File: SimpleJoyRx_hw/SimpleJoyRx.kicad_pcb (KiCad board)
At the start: 2 copper layers, 20 x 50 mm, 111 parts, among them Q1 IRF9358, Q2 2N7002, Q3 IRLML0030, Q4 IRLML0030, SW1 DIPx8, SW2 BUTTON, SW3 1P2T, U1 USBLC6

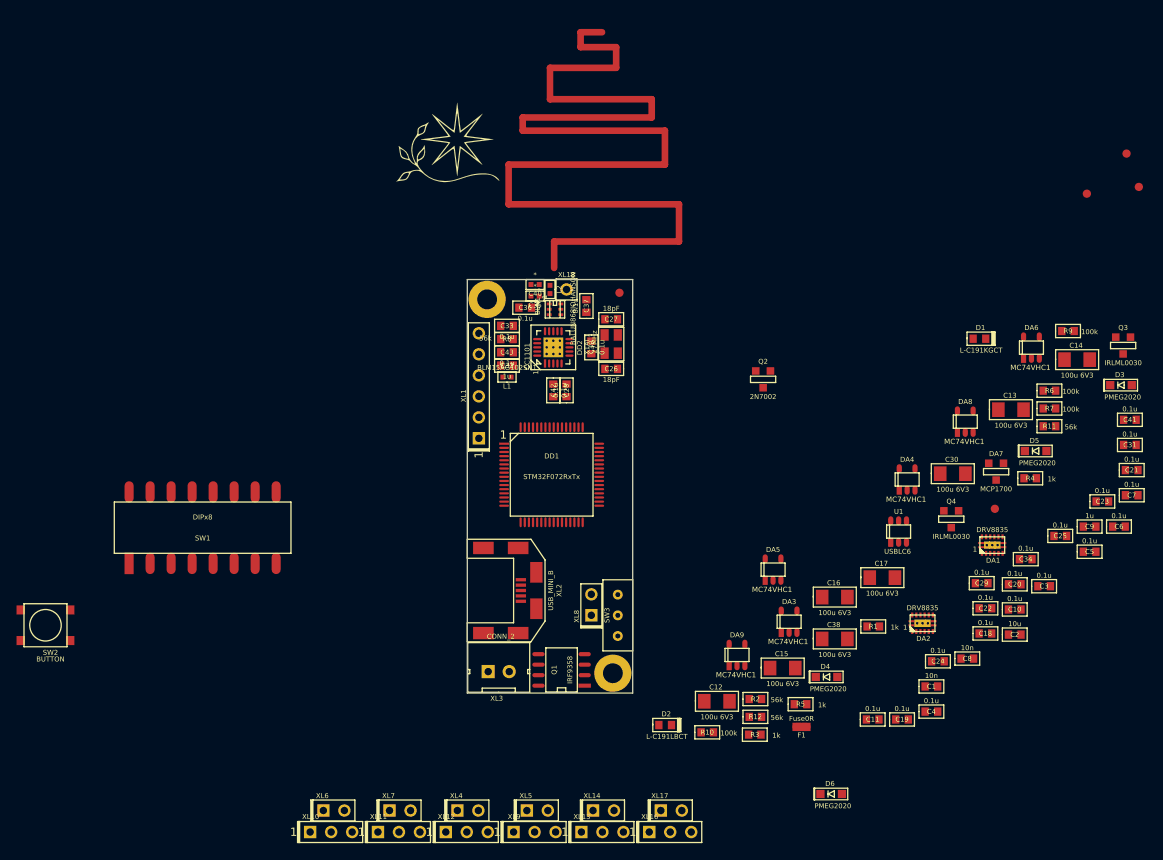
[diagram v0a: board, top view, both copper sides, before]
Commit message: RX layout done
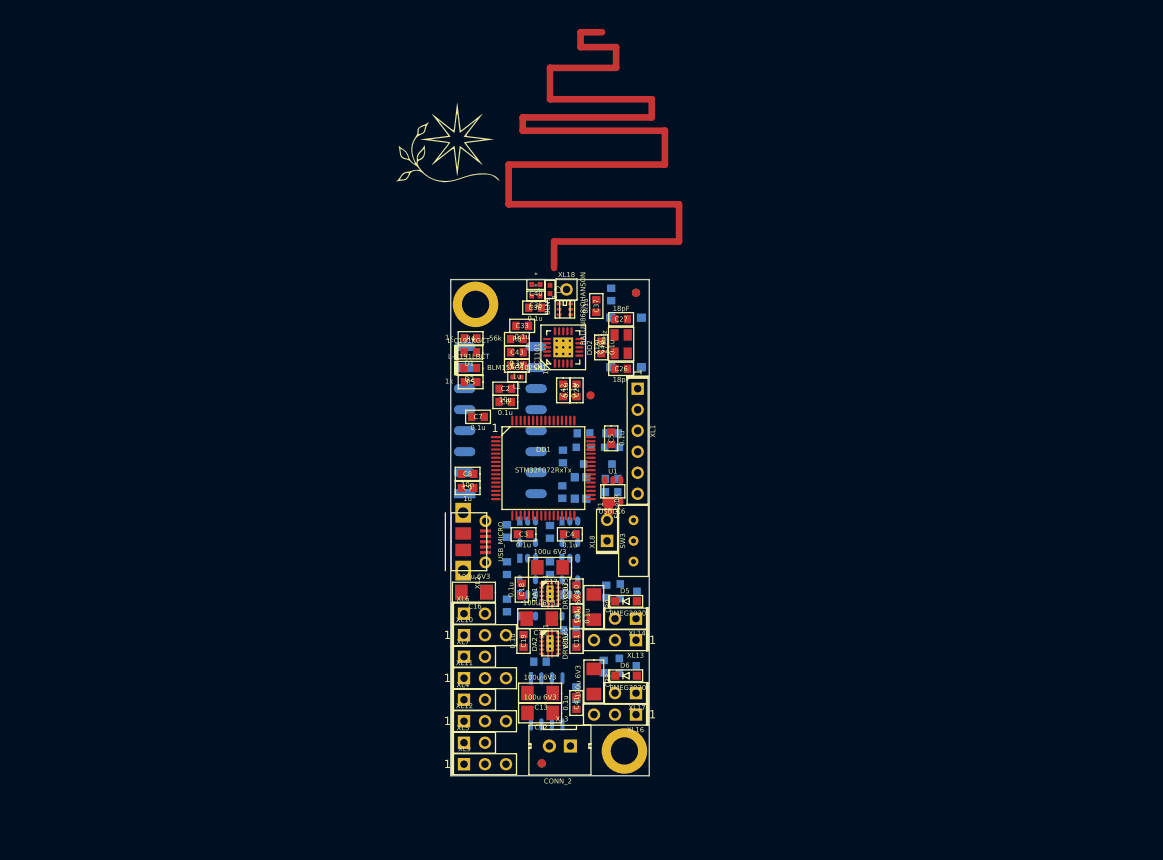
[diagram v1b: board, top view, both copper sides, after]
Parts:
- C1, C14, C20, C21, C22, C23, C24, C25, C29, C34, D3, D4, DA3, DA4, DA5, DA6, DA7, DA8, DA9, Q1, Q2, Q3, Q4, R1, R10, R11, R12, R2, R3, R6, R7, R9, RP3, RP4, SW1, SW2: moved to B.Cu
- HOLE1, HOLE2: footprint PCB:Hole2d4_out4d5mm -> PCB:Hole3d3_out5d5mm
- XL2: value USB_MINI_B -> USB_MICRO; footprint Connectors:USBmicro_MOLEX_WM17142 -> Connectors:USBmicro_MOLEX_1050170001
- moved RP4 100.4 mm to (135.0, 128.5)
- moved RP2 95.3 mm to (135.0, 128.5)
- moved C7 79.6 mm to (127.3, 86.6), turned to 180 degrees
- moved C14 78.2 mm to (126.8, 107.8), turned to 180 degrees
- moved SW2 78.1 mm to (145.2, 77.6), turned to 270 degrees
- moved C21 75.9 mm to (130.8, 100.4), turned to 90 degrees
- moved C6 75.7 mm to (130.6, 84.8), turned to 180 degrees
- moved C9 75.4 mm to (126.0, 95.2), turned to 180 degrees
- moved C41 75.2 mm to (139.2, 121.2), turned to 90 degrees
- moved C23 73.1 mm to (130.8, 109.4), turned to 90 degrees
- moved C31 70.0 mm to (139.2, 110.7), turned to 270 degrees
- moved R4 69.7 mm to (126.4, 77.1), turned to 180 degrees
- moved DA6 68.4 mm to (133.3, 109.4)
- moved C2 68.4 mm to (130.6, 83.2), turned to 180 degrees
- moved R6 67.9 mm to (139.2, 120.0), turned to 270 degrees
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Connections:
- HOLE2 pad H: GND -> GNDPWR
- XL2 pad H2: Net-(XL2-PadH2) -> (no net)
- XL2 pad H3: Net-(XL2-PadH3) -> (no net)
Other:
- board size 20 x 50 mm -> 24 x 60 mm
- net class Default: trace_width 0.25 -> 0.2

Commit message: Rx tracing done
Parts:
- F1: moved to B.Cu
- moved F1 12.6 mm to (130.5, 97.5)
- moved Logo1 12.0 mm to (135.5, 55.0)
- moved ANT1 4.85 mm to (136.2, 69.7)
- moved C26 3.19 mm to (146.9, 78.6), turned to 90 degrees
- moved C7 2.77 mm to (126.1, 89.1)
- moved XL8 2.66 mm to (142.9, 104.3)
- moved C18 2.60 mm to (131.9, 105.0), turned to 0 degrees
- moved C10 1.84 mm to (140.1, 106.1), turned to 180 degrees
- moved R9 1.54 mm to (143.8, 97.2)
- moved R4 1.50 mm to (127.9, 77.1), turned to 0 degrees
- moved R1 1.42 mm to (136.2, 116.5), turned to 0 degrees
- moved TP1 1.41 mm to (140.8, 82.6)
- moved C15 1.29 mm to (135.9, 111.5)
- moved C40 1.20 mm to (135.5, 70.7)
- moved C35 1.20 mm to (135.5, 72.0)
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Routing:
- net PwrUnst: track 0.00 -> 218.3 mm, vias 0 -> 7
- net GND: track 0.00 -> 212.4 mm, vias 0 -> 28
- net GNDPWR: track 0.00 -> 203.5 mm, vias 0 -> 8
- net /ANT2: track 0.00 -> 147.7 mm
- net +3.3V: track 0.00 -> 119.4 mm, vias 0 -> 6
- net VCC: track 0.00 -> 54.8 mm, vias 0 -> 5
- net +BATT: track 0.00 -> 42.8 mm, vias 0 -> 3
- net /PWM6: track 0.00 -> 28.7 mm, vias 0 -> 2
- net Net-(Q1-Pad4): track 0.00 -> 28.4 mm, vias 0 -> 1
- net /DIR2: track 0.00 -> 28.2 mm, vias 0 -> 2
- net /PWM2: track 0.00 -> 28.1 mm, vias 0 -> 2
- net /PWM1: track 0.00 -> 28.1 mm, vias 0 -> 2
- net /DIR1: track 0.00 -> 27.9 mm, vias 0 -> 2
- net /CC_CS: track 0.00 -> 27.5 mm, vias 0 -> 2
- net /CC_GDO0: track 0.00 -> 27.4 mm, vias 0 -> 2
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- added copper zone on B.Cu, net +BATT
- added copper zone on B.Cu, net /PRE_BAT_PWR
- added copper zone on B.Cu, net GND
- added copper zone on F.Cu, net GND
- added copper zone on In1.Cu, net GND
- added copper zone on In2.Cu, net GND
- added copper zone on B.Cu, net GNDPWR
- added copper zone on F.Cu, net GNDPWR
- added copper zone on In1.Cu, net GNDPWR
- added copper zone on In2.Cu, net GNDPWR
- added copper zone on B.Cu, net PwrUnst
- added copper zone on F.Cu, net PwrUnst
- added copper zone on In1.Cu, net PwrUnst
- added copper zone on In2.Cu, net PwrUnst
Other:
- board size 24 x 60 mm -> 24 x 90 mm
- copper layers 2 -> 4
- net class Default: clearance 0.2 -> 0.21; trace_width 0.2 -> 0.25; via_dia 0.8 -> 0.7; via_drill 0.4 -> 0.3
- net class Wide added: clearance 0.21, trace_width 0.6, via_dia 0.9, via_drill 0.4
- rule trace_clearance: 0.2 -> 0.21
- rule trace_min: 0.2 -> 0.1
- rule via_min_drill: 0.3 -> 0.2
- rule via_min_size: 0.4 -> 0.3

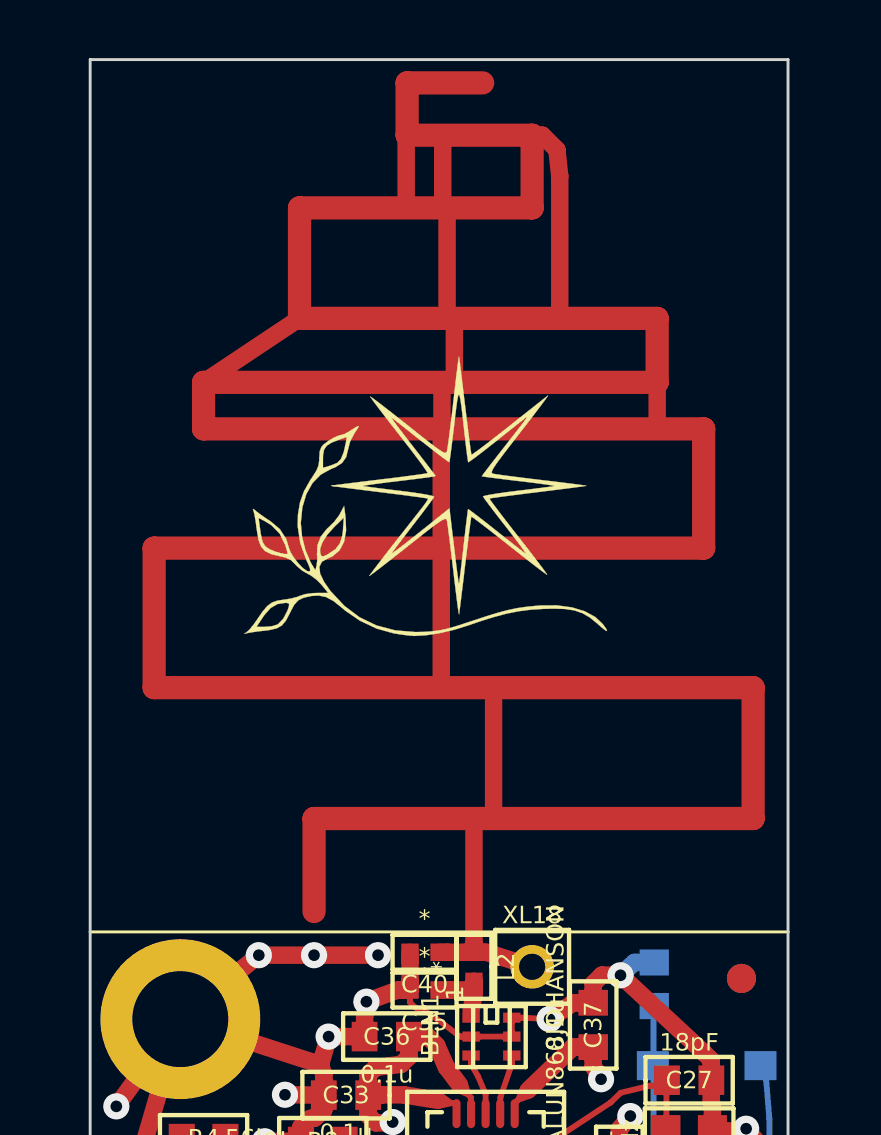
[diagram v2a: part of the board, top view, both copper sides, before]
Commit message: + Antenna
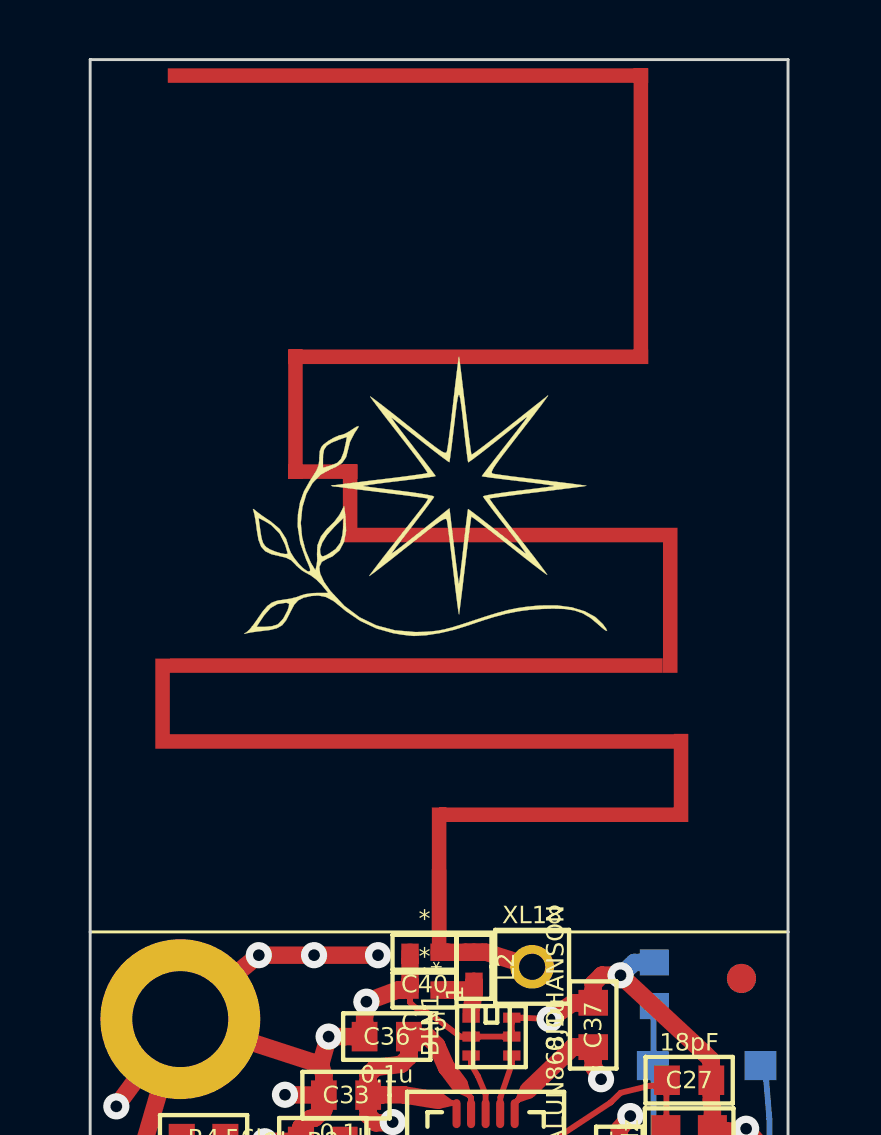
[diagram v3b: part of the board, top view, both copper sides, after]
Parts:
- ANT1: footprint Radio:ANT_868_SEIDHE -> Radio:ANT_868_24x30
- moved ANT1 0.36 mm to (136.0, 70.0), turned to 180 degrees
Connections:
- DD1 pad 2: (no net) -> Net-(DD1-Pad2)
- DD1 pad 26: (no net) -> Net-(DD1-Pad26)
- DD1 pad 3: (no net) -> Net-(DD1-Pad3)
- DD1 pad 4: (no net) -> Net-(DD1-Pad4)
- DD1 pad 5: (no net) -> Net-(DD1-Pad5)
- DD1 pad 50: (no net) -> Net-(DD1-Pad50)
- DD1 pad 51: (no net) -> Net-(DD1-Pad51)
- DD1 pad 52: (no net) -> Net-(DD1-Pad52)
- DD1 pad 53: (no net) -> Net-(DD1-Pad53)
- DD1 pad 54: (no net) -> Net-(DD1-Pad54)
- DD1 pad 6: (no net) -> Net-(DD1-Pad6)
- DD1 pad 7: (no net) -> Net-(DD1-Pad7)
- DD2 pad 3: Net-(DD2-Pad3) -> (no net)
- SW3 pad 3: Net-(SW3-Pad3) -> (no net)
- XL2 pad H2: (no net) -> Net-(XL2-PadH2)
- XL2 pad H3: (no net) -> Net-(XL2-PadH3)
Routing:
- net /ANT2: track 147.7 -> 6.12 mm
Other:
- net class Wide05 added: clearance 0.21, trace_width 0.5, via_dia 0.7, via_drill 0.3

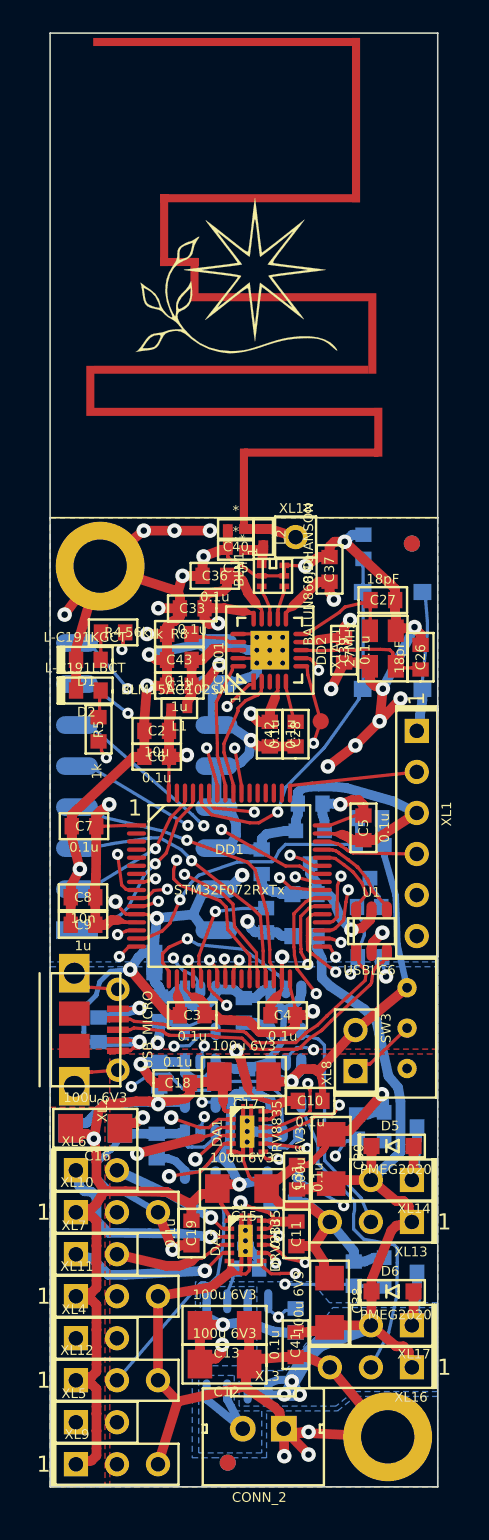
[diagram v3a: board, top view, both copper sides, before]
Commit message: RX PCB seems done
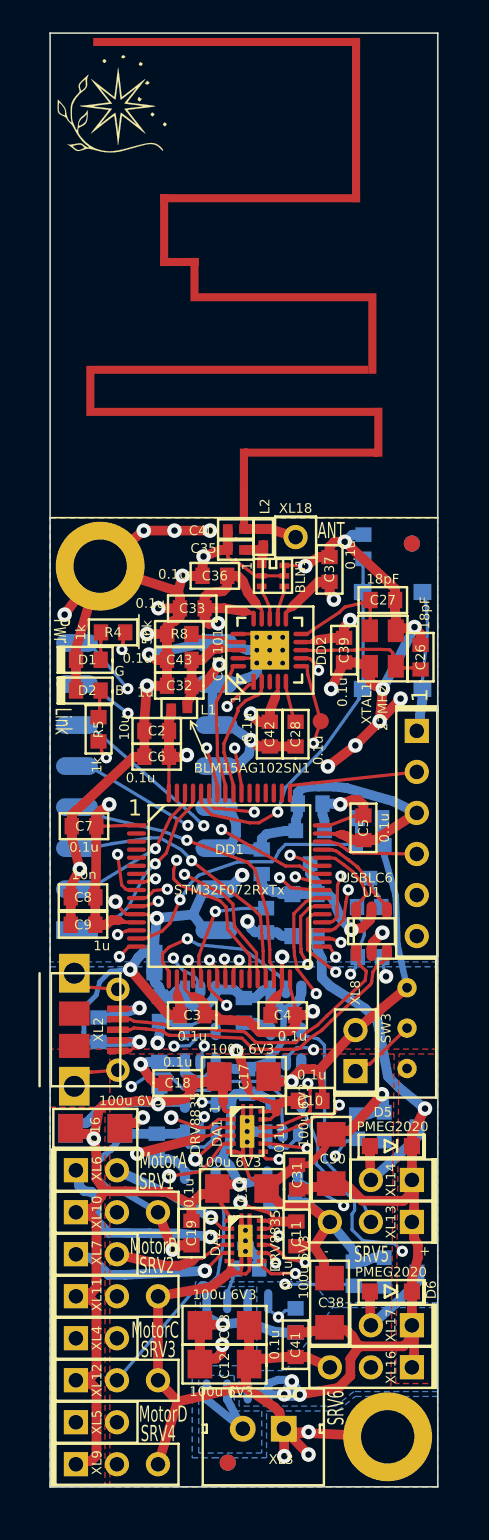
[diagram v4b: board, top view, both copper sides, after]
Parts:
- added Logo2: Logo, Pictures:Livetronic27x9, B.Cu at (134.0, 54.4)
- Logo1: footprint Pictures:Ostranna_12d7_10d1 -> Pictures:Ostranna_8x8
- moved Logo1 12.7 mm to (128.2, 44.6)
- moved D5 0.10 mm to (145.1, 108.9), turned to 180 degrees
- moved D6 0.10 mm to (145.1, 117.9), turned to 180 degrees
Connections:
- DD1 pad 2: Net-(DD1-Pad2) -> (no net)
- DD1 pad 26: Net-(DD1-Pad26) -> (no net)
- DD1 pad 3: Net-(DD1-Pad3) -> (no net)
- DD1 pad 4: Net-(DD1-Pad4) -> (no net)
- DD1 pad 5: Net-(DD1-Pad5) -> (no net)
- DD1 pad 50: Net-(DD1-Pad50) -> (no net)
- DD1 pad 51: Net-(DD1-Pad51) -> (no net)
- DD1 pad 52: Net-(DD1-Pad52) -> (no net)
- DD1 pad 53: Net-(DD1-Pad53) -> (no net)
- DD1 pad 54: Net-(DD1-Pad54) -> (no net)
- DD1 pad 6: Net-(DD1-Pad6) -> (no net)
- DD1 pad 7: Net-(DD1-Pad7) -> (no net)
- DD2 pad 3: (no net) -> Net-(DD2-Pad3)
- SW3 pad 3: (no net) -> Net-(SW3-Pad3)
- XL14 pad 1: /PWM_OUT5 -> PwrUnst
- XL14 pad 2: PwrUnst -> /PWM_OUT5
- XL17 pad 1: /PWM_OUT6 -> PwrUnst
- XL17 pad 2: PwrUnst -> /PWM_OUT6
- XL2 pad H2: Net-(XL2-PadH2) -> (no net)
- XL2 pad H3: Net-(XL2-PadH3) -> (no net)
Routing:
- net GNDPWR: track 203.5 -> 194.9 mm
- net PwrUnst: track 218.3 -> 210.0 mm, vias 7 -> 8
- net VCC: track 54.8 -> 60.0 mm
- net +3.3V: track 119.4 -> 123.1 mm
- net GND: track 212.4 -> 214.3 mm
- net /PWM_OUT6: track 5.46 -> 6.65 mm
- net /PWM_OUT5: track 5.46 -> 6.65 mm
- net /MOTORB1: track 8.26 -> 9.14 mm
- net /MOTORC2: track 21.5 -> 22.4 mm
- net Net-(DA9-Pad4): track 19.7 -> 20.2 mm, vias 0 -> 1
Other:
- board text added: "+"
- board text added: "-"
- board text added: "ANT"
- board text added: "B"
- board text added: "BOOTLOADER"
- board text added: "DEBUG"
- board text added: "G"
- board text added: "Link"
- board text added: "MotorA"
- board text added: "MotorB"
- board text added: "MotorC"
- board text added: "MotorD"
- board text added: "PWM5"
- board text added: "PWM6"
- board text added: "PWR Switch"
- board text added: "Pwr"
- board text added: "SRV1"
- board text added: "SRV2"
- board text added: "SRV3"
- board text added: "SRV4"
- board text added: "SRV5"
- board text added: "SRV6"
- board text added: "SimpleJoy RX 1.0"

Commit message: TX layout started
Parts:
- added Logo3: Logo, Pictures:Livetronic13x4, B.Cu at (139.5, 78.7)
- Logo1: moved to B.Cu
- Logo2: moved to F.Cu
- moved Logo2 6.71 mm to (140.7, 54.7)
- moved Logo1 1.28 mm to (129.2, 45.4), turned to 270 degrees
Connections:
- DD1 pad 2: (no net) -> Net-(DD1-Pad2)
- DD1 pad 26: (no net) -> Net-(DD1-Pad26)
- DD1 pad 3: (no net) -> Net-(DD1-Pad3)
- DD1 pad 4: (no net) -> Net-(DD1-Pad4)
- DD1 pad 5: (no net) -> Net-(DD1-Pad5)
- DD1 pad 50: (no net) -> Net-(DD1-Pad50)
- DD1 pad 51: (no net) -> Net-(DD1-Pad51)
- DD1 pad 52: (no net) -> Net-(DD1-Pad52)
- DD1 pad 53: (no net) -> Net-(DD1-Pad53)
- DD1 pad 54: (no net) -> Net-(DD1-Pad54)
- DD1 pad 6: (no net) -> Net-(DD1-Pad6)
- DD1 pad 7: (no net) -> Net-(DD1-Pad7)
- DD2 pad 3: Net-(DD2-Pad3) -> (no net)
- SW3 pad 3: Net-(SW3-Pad3) -> (no net)
- XL2 pad H2: (no net) -> Net-(XL2-PadH2)
- XL2 pad H3: (no net) -> Net-(XL2-PadH3)
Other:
- board text removed: "BOOTLOADER"
